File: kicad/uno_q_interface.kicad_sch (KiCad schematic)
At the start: 0 parts

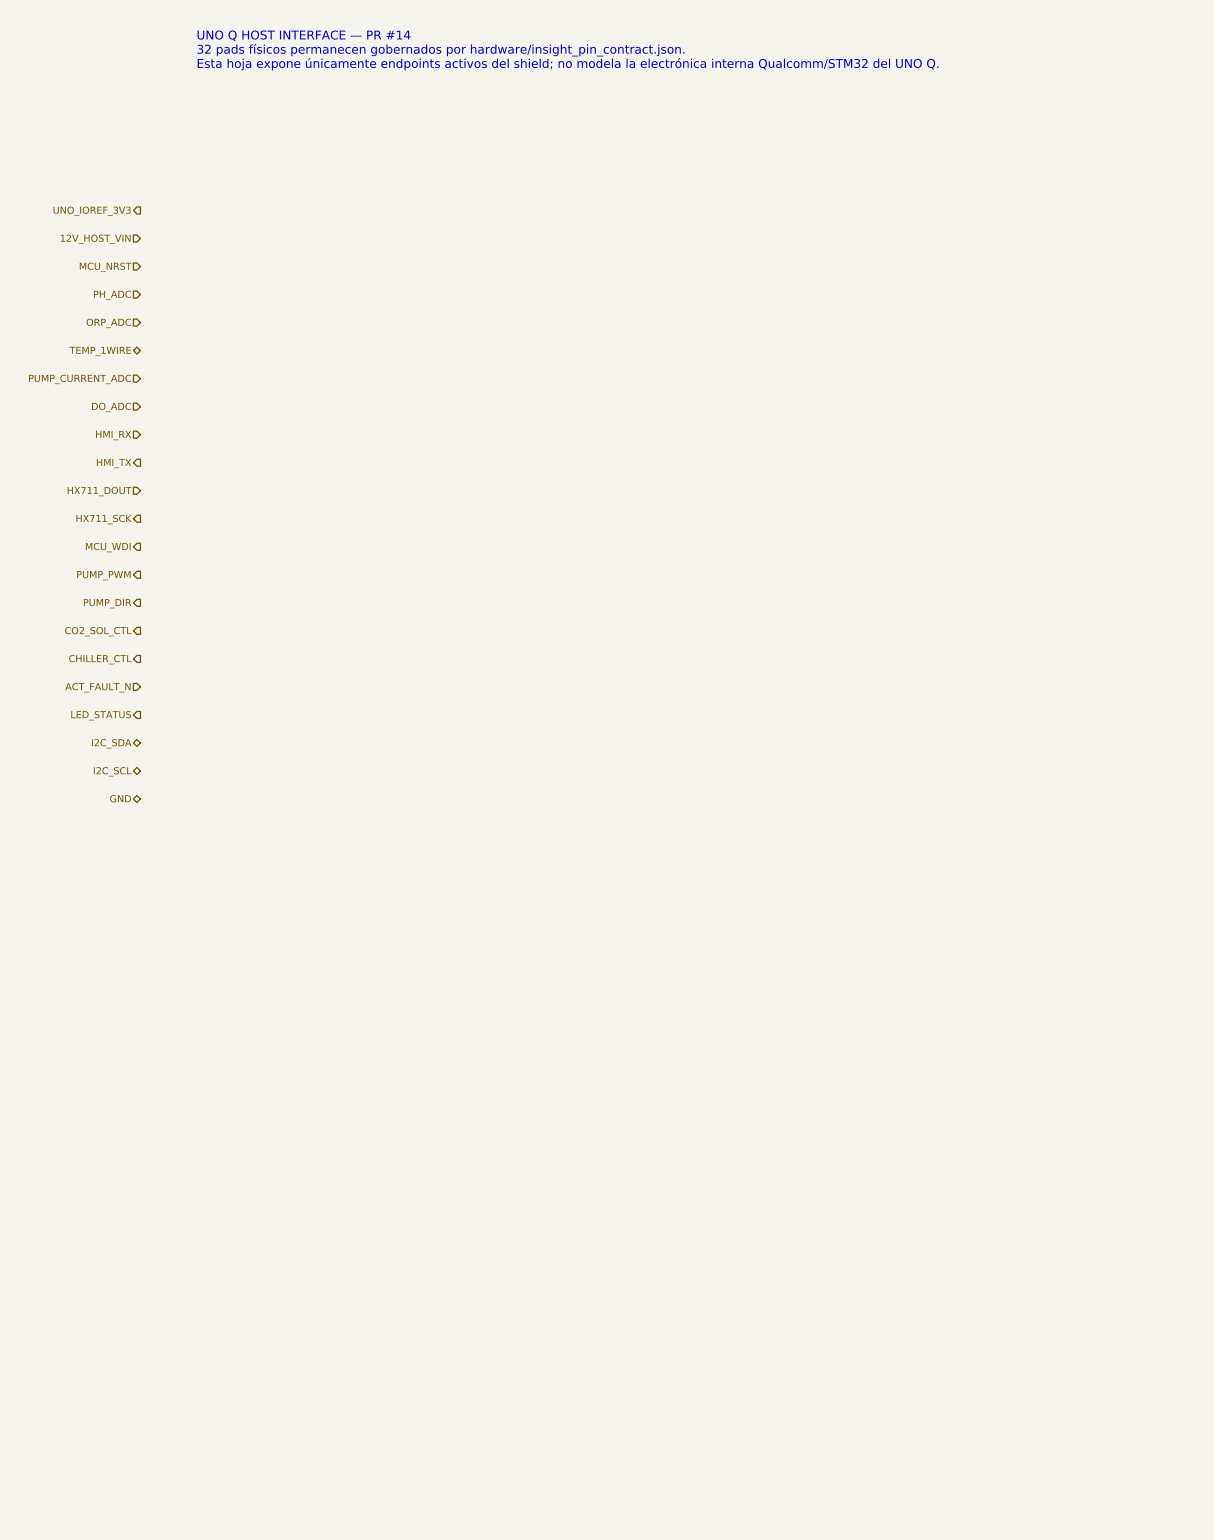
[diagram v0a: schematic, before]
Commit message: eda: materializar hierarchy de producción y cerrar ERC en cero (#15)
Materializa Z0–Z4 de forma determinista desde JSON/BOM, registra NFB_GEN, cierra seis links físicos verificados, elimina la deuda ERC de PR #14 y congela ERC=0/0 antes de placement. Mantiene placement, routing y geometría PCB fuera de alcance.
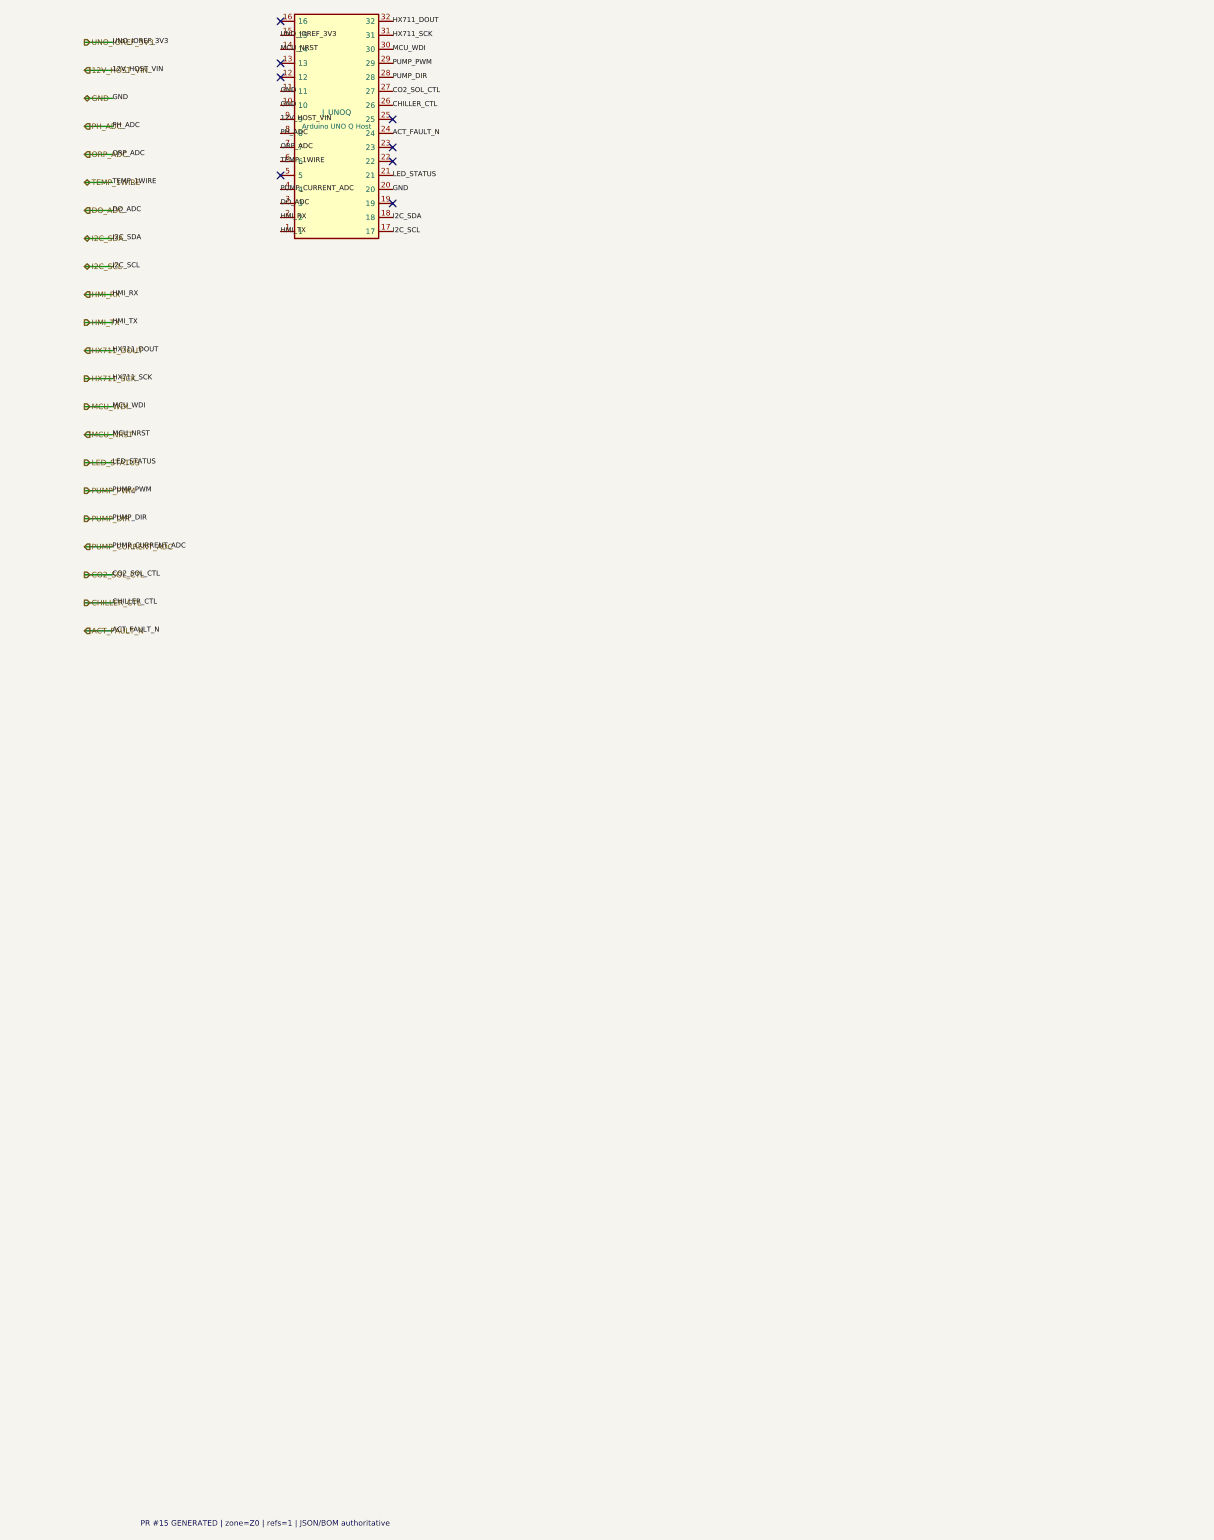
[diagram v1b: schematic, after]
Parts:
- added J_UNOQ: Arduino UNO Q Host, NFB:Arduino_UNO_Q_Carrier_Rotated, symbol NFB_GEN:SYM_J_UNOQ
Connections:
- net 12V_HOST_VIN: now also J_UNOQ.9
- net ACT_FAULT_N: now also J_UNOQ.24
- net CHILLER_CTL: now also J_UNOQ.26
- net CO2_SOL_CTL: now also J_UNOQ.27
- net DO_ADC: now also J_UNOQ.3
- net GND: now also J_UNOQ.10, J_UNOQ.11, J_UNOQ.20
- net HMI_RX: now also J_UNOQ.2
- net HMI_TX: now also J_UNOQ.1
- net HX711_DOUT: now also J_UNOQ.32
- net HX711_SCK: now also J_UNOQ.31
- net I2C_SCL: now also J_UNOQ.17
- net I2C_SDA: now also J_UNOQ.18
- net LED_STATUS: now also J_UNOQ.21
- net MCU_NRST: now also J_UNOQ.14
- net MCU_WDI: now also J_UNOQ.30
- net ORP_ADC: now also J_UNOQ.7
- net PH_ADC: now also J_UNOQ.8
- net PUMP_CURRENT_ADC: now also J_UNOQ.4
- net PUMP_DIR: now also J_UNOQ.28
- net PUMP_PWM: now also J_UNOQ.29
- net TEMP_1WIRE: now also J_UNOQ.6
- net UNO_IOREF_3V3: now also J_UNOQ.15
- no-connect marks 0 -> 8
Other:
- note added: "PR #15 GENERATED | zone=Z0 | refs=1 | JSON/BOM authoritative"
- note removed: "UNO Q HOST INTERFACE — PR #14 32 pads físicos permanecen gobernados por hardware/insight_pin_contract.json. Esta hoja expone únicamente endpoints activos del shield; no modela la electrónica interna Qualcomm/STM32 del UNO Q."
- title: NFB Insight PCBA v2 — UNO Q Interface -> NFB Insight PCBA v2 — Z0 GENERATED PRODUCTION
